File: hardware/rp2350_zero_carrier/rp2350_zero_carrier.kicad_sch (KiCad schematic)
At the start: 19 parts, among them J1 RP2350_Zero_Header_23p, J2 USB_A_Neltron_5075AR-04-WH, J3 RP2350_Zero_Header_23p, SW1 SW_SPDT_NKK_115643_Slide, SW2 SW_SPDT_NKK_115643_Slide, SW3 SW_SPDT_NKK_115643_Slide, SW4 SW_SPDT_NKK_115643_Slide, SW5 SW_SPDT_NKK_115643_Slide, SW6 SW_TACT_Akizuki_DTS63, U1 TPS2553DBVR

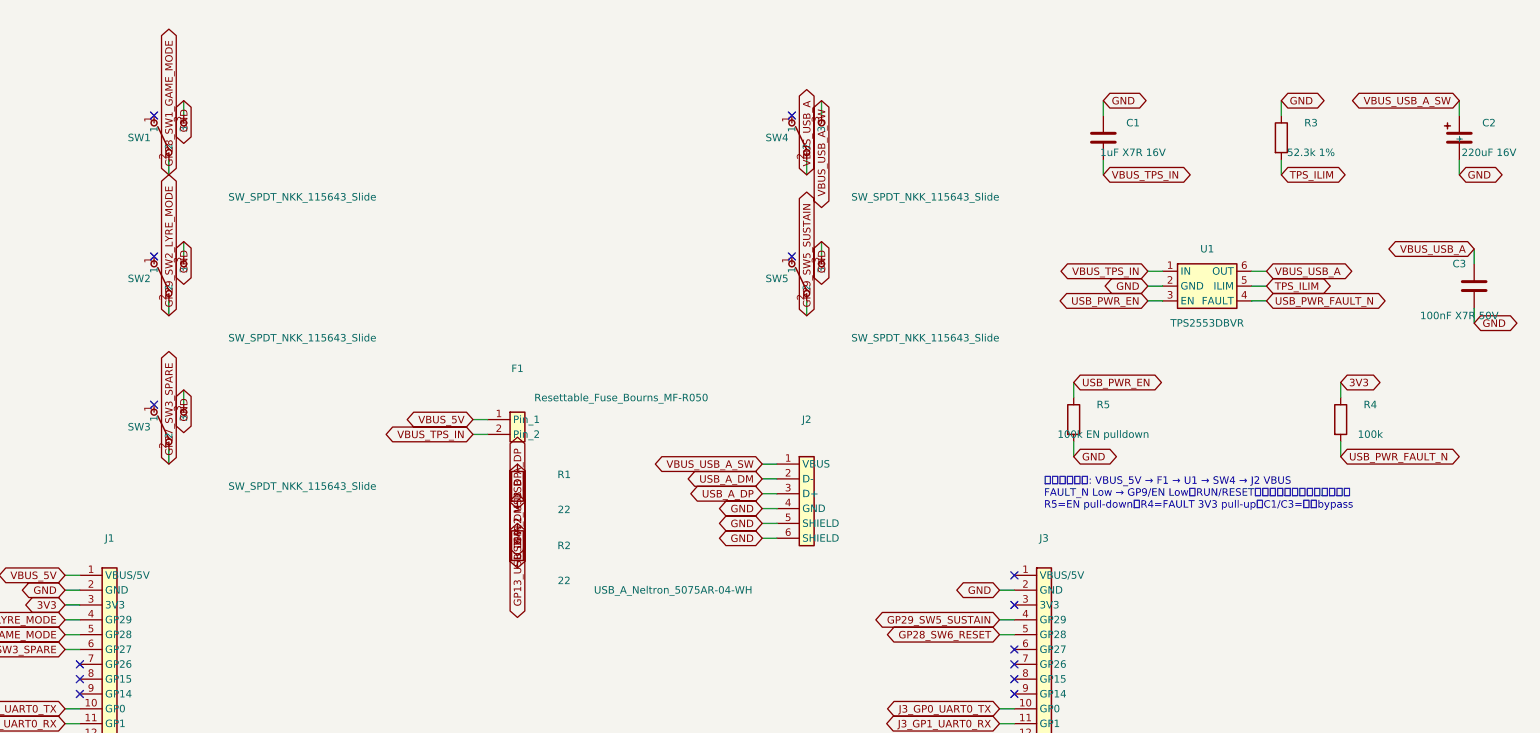
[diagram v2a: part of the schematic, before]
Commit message: Fix schematic visual audit readability
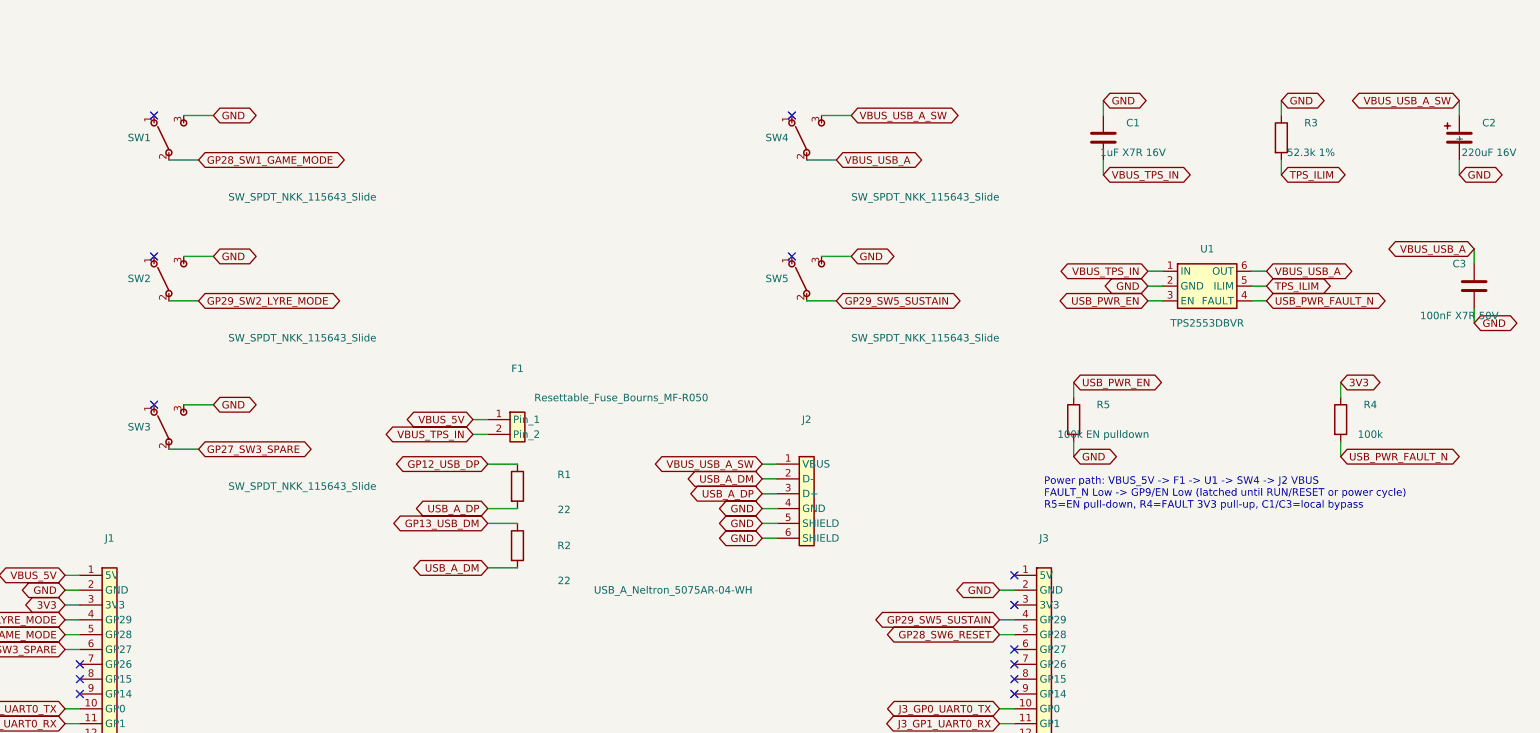
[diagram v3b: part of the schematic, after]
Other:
- note added: "Power path: VBUS_5V -> F1 -> U1 -> SW4 -> J2 VBUS FAULT_N Low -> GP9/EN Low (latched until RUN/RESET or power cycle) R5=EN pull-down, R4=FAULT 3V3 pull-up, C1/C3=local bypass"
- note removed: "電源ブロック: VBUS_5V → F1 → U1 → SW4 → J2 VBUS FAULT_N Low → GP9/EN Low（RUN/RESETまたは電源再投入まで保持） R5=EN pull-down、R4=FAULT 3V3 pull-up、C1/C3=局所bypass"
- moved on the sheet: J1, J3
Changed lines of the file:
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@@
   (wire (pts (xy 251.46 82.55) (xy 251.46 85.09)) (stroke (width 0) (type default)) (uuid "b1c9a1a0-w011-4a00-9000-000000000001"))
   (global_label "USB_PWR_FAULT_N" (shape bidirectional) (at 251.46 85.09 0) (effects (font (size 1.27 1.27)) (justify left)) (uuid "b1c9a1a0-l011-4a00-9000-000000000001"))
-  (text "電源ブロック: VBUS_5V → F1 → U1 → SW4 → J2 VBUS\nFAULT_N Low → GP9/EN Low（RUN/RESETまたは電源再投入まで保持）\nR5=EN pull-down、R4=FAULT 3V3 pull-up、C1/C3=局所bypass"
+  (text "Power path: VBUS_5V -> F1 -> U1 -> SW4 -> J2 VBUS\nFAULT_N Low -> GP9/EN Low (latched until RUN/RESET or power cycle)\nR5=EN pull-down, R4=FAULT 3V3 pull-up, C1/C3=local bypass"
     (at 200.66 91.44 0)
     (effects (font (size 1.27 1.27)) (justify left))
@@
   (no_connect (at 195.58 158.75))
   (no_connect (at 195.58 161.29))
-  (global_label "GP12_USB_DP" (shape bidirectional) (at 110.49 86.36 90) (effects (font (size 1.27 1.27)) (justify right)))
-  (global_label "USB_A_DP" (shape bidirectional) (at 110.49 93.98 90) (effects (font (size 1.27 1.27)) (justify left)))
-  (global_label "GP13_USB_DM" (shape bidirectional) (at 110.49 96.52 90) (effects (font (size 1.27 1.27)) (justify right)))
-  (global_label "USB_A_DM" (shape bidirectional) (at 110.49 104.14 90) (effects (font (size 1.27 1.27)) (justify left)))
+  (wire (pts (xy 110.49 86.36) (xy 105.41 86.36)) (stroke (width 0) (type default)))
+  (global_label "GP12_USB_DP" (shape bidirectional) (at 105.41 86.36 0) (effects (font (size 1.27 1.27)) (justify right)))
+  (wire (pts (xy 110.49 93.98) (xy 105.41 93.98)) (stroke (width 0) (type default)))
+  (global_label "USB_A_DP" (shape bidirectional) (at 105.41 93.98 0) (effects (font (size 1.27 1.27)) (justify right)))
+  (wire (pts (xy 110.49 96.52) (xy 105.41 96.52)) (stroke (width 0) (type default)))
+  (global_label "GP13_USB_DM" (shape bidirectional) (at 105.41 96.52 0) (effects (font (size 1.27 1.27)) (justify right)))
+  (wire (pts (xy 110.49 104.14) (xy 105.41 104.14)) (stroke (width 0) (type default)))
+  (global_label "USB_A_DM" (shape bidirectional) (at 105.41 104.14 0) (effects (font (size 1.27 1.27)) (justify right)))
   (wire (pts (xy 105.41 78.74) (xy 102.87 78.74)) (stroke (width 0) (type default)))
   (global_label "VBUS_5V" (shape bidirectional) (at 102.87 78.74 0) (effects (font (size 1.27 1.27)) (justify right)))
@@
   (global_label "GND" (shape bidirectional) (at 152.4 99.06 0) (effects (font (size 1.27 1.27)) (justify right)))
   (no_connect (at 48.26 26.67))
-  (wire (pts (xy 50.8 34.29) (xy 50.8 36.83)) (stroke (width 0) (type default)))
-  (global_label "GP28_SW1_GAME_MODE" (shape bidirectional) (at 50.8 36.83 90) (effects (font (size 1.27 1.27)) (justify left)))
-  (wire (pts (xy 53.34 26.67) (xy 53.34 24.13)) (stroke (width 0) (type default)))
-  (global_label "GND" (shape bidirectional) (at 53.34 24.13 90) (effects (font (size 1.27 1.27)) (justify right)))
+  (wire (pts (xy 50.8 34.29) (xy 55.88 34.29)) (stroke (width 0) (type default)))
+  (global_label "GP28_SW1_GAME_MODE" (shape bidirectional) (at 55.88 34.29 0) (effects (font (size 1.27 1.27)) (justify left)))
+  (wire (pts (xy 53.34 26.67) (xy 58.42 26.67)) (stroke (width 0) (type default)))
+  (global_label "GND" (shape bidirectional) (at 58.42 26.67 0) (effects (font (size 1.27 1.27)) (justify left)))
   (no_connect (at 48.26 50.8))
-  (wire (pts (xy 50.8 58.42) (xy 50.8 60.96)) (stroke (width 0) (type default)))
-  (global_label "GP29_SW2_LYRE_MODE" (shape bidirectional) (at 50.8 60.96 90) (effects (font (size 1.27 1.27)) (justify left)))
-  (wire (pts (xy 53.34 50.8) (xy 53.34 48.26)) (stroke (width 0) (type default)))
-  (global_label "GND" (shape bidirectional) (at 53.34 48.26 90) (effects (font (size 1.27 1.27)) (justify right)))
+  (wire (pts (xy 50.8 58.42) (xy 55.88 58.42)) (stroke (width 0) (type default)))
+  (global_label "GP29_SW2_LYRE_MODE" (shape bidirectional) (at 55.88 58.42 0) (effects (font (size 1.27 1.27)) (justify left)))
+  (wire (pts (xy 53.34 50.8) (xy 58.42 50.8)) (stroke (width 0) (type default)))
+  (global_label "GND" (shape bidirectional) (at 58.42 50.8 0) (effects (font (size 1.27 1.27)) (justify left)))
   (no_connect (at 48.26 76.2))
-  (wire (pts (xy 50.8 83.82) (xy 50.8 86.36)) (stroke (width 0) (type default)))
-  (global_label "GP27_SW3_SPARE" (shape bidirectional) (at 50.8 86.36 90) (effects (font (size 1.27 1.27)) (justify left)))
-  (wire (pts (xy 53.34 76.2) (xy 53.34 73.66)) (stroke (width 0) (type default)))
-  (global_label "GND" (shape bidirectional) (at 53.34 73.66 90) (effects (font (size 1.27 1.27)) (justify right)))
+  (wire (pts (xy 50.8 83.82) (xy 55.88 83.82)) (stroke (width 0) (type default)))
+  (global_label "GP27_SW3_SPARE" (shape bidirectional) (at 55.88 83.82 0) (effects (font (size 1.27 1.27)) (justify left)))
+  (wire (pts (xy 53.34 76.2) (xy 58.42 76.2)) (stroke (width 0) (type default)))
+  (global_label "GND" (shape bidirectional) (at 58.42 76.2 0) (effects (font (size 1.27 1.27)) (justify left)))
   (no_connect (at 157.48 26.67))
-  (wire (pts (xy 160.02 34.29) (xy 160.02 36.83)) (stroke (width 0) (type default)))
-  (global_label "VBUS_USB_A" (shape bidirectional) (at 160.02 36.83 90) (effects (font (size 1.27 1.27)) (justify left)))
-  (wire (pts (xy 162.56 26.67) (xy 162.56 24.13)) (stroke (width 0) (type default)))
-  (global_label "VBUS_USB_A_SW" (shape bidirectional) (at 162.56 24.13 90) (effects (font (size 1.27 1.27)) (justify right)))
+  (wire (pts (xy 160.02 34.29) (xy 165.1 34.29)) (stroke (width 0) (type default)))
+  (global_label "VBUS_USB_A" (shape bidirectional) (at 165.1 34.29 0) (effects (font (size 1.27 1.27)) (justify left)))
+  (wire (pts (xy 162.56 26.67) (xy 167.64 26.67)) (stroke (width 0) (type default)))
+  (global_label "VBUS_USB_A_SW" (shape bidirectional) (at 167.64 26.67 0) (effects (font (size 1.27 1.27)) (justify left)))
   (no_connect (at 157.48 50.8))
-  (wire (pts (xy 160.02 58.42) (xy 160.02 60.96)) (stroke (width 0) (type default)))
-  (global_label "GP29_SW5_SUSTAIN" (shape bidirectional) (at 160.02 60.96 90) (effects (font (size 1.27 1.27)) (justify left)))
-  (wire (pts (xy 162.56 50.8) (xy 162.56 48.26)) (stroke (width 0) (type default)))
-  (global_label "GND" (shape bidirectional) (at 162.56 48.26 90) (effects (font (size 1.27 1.27)) (justify right)))
+  (wire (pts (xy 160.02 58.42) (xy 165.1 58.42)) (stroke (width 0) (type default)))
+  (global_label "GP29_SW5_SUSTAIN" (shape bidirectional) (at 165.1 58.42 0) (effects (font (size 1.27 1.27)) (justify left)))
+  (wire (pts (xy 162.56 50.8) (xy 167.64 50.8)) (stroke (width 0) (type default)))
+  (global_label "GND" (shape bidirectional) (at 167.64 50.8 0) (effects (font (size 1.27 1.27)) (justify left)))
   (wire (pts (xy 154.94 146.05) (xy 152.4 146.05)) (stroke (width 0) (type default)))
   (global_label "GND" (shape bidirectional) (at 152.4 146.05 0) (effects (font (size 1.27 1.27)) (justify right)))
